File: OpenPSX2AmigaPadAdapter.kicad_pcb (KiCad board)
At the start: 2 copper layers, 58.9 x 44.2 mm, 36 parts, among them J1 TO_PSX_PAD, J2 DB9_F, J3 CONN_FTDI, J4 CONN_ICSP, J99 OSHW_LOGO, Q1 BSS138, Q2 BSS138, Q3 BSS138, Q4 BSS138, SW1 RESET, U1 ATmega328P-AU, U2 LM1117-3.3, Y1 16MHz

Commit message: Add license
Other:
- board text added: "Licensed under CERN OHL v.1.2"
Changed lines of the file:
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@@
   (general
     (thickness 1.6)
-    (drawings 26)
-    (tracks 340)
+    (drawings 27)
+    (tracks 339)
     (zones 0)
     (modules 36)
@@
   (title_block
     (title OpenPSX2AmigaPadAdapter)
-    (date 2019-09-11)
+    (date 2019-09-14)
     (rev 1git)
     (company SukkoPera)
+    (comment 1 "Licensed under CERN OHL v.1.2")
   )
   (layers
@@
     )
   )
+  (gr_text "Licensed under CERN OHL v.1.2" (at 141.986 90.424) (layer B.SilkS)
+    (effects (font (size 1 1) (thickness 0.15)) (justify mirror))
+  )
   (gr_circle (center 143.002 79.248) (end 143.129 79.248) (layer F.SilkS) (width 0.4))
   (gr_text NC (at 132.08 90.424) (layer F.SilkS)
@@
   (segment (start 143.002 65.024) (end 142.494 64.516) (width 0.25) (layer B.Cu) (net 7))
   (segment (start 125.39 64.944) (end 131.15 64.944) (width 0.25) (layer F.Cu) (net 7))
-  (via (at 125.39 61.468) (size 0.6) (drill 0.4) (layers F.Cu B.Cu) (net 7))
-  (segment (start 125.39 61.892264) (end 125.39 64.944) (width 0.25) (layer F.Cu) (net 7))
+  (via (at 125.39 61.595) (size 0.6) (drill 0.4) (layers F.Cu B.Cu) (net 7))
   (segment (start 136.652 84.582) (end 136.652 82.677) (width 0.25) (layer F.Cu) (net 7))
   (segment (start 136.652 85.09) (end 136.652 84.582) (width 0.25) (layer F.Cu) (net 7))
   (segment (start 136.271 85.471) (end 136.652 85.09) (width 0.25) (layer F.Cu) (net 7))
   (segment (start 125.222 85.471) (end 136.271 85.471) (width 0.25) (layer F.Cu) (net 7))
-  (segment (start 125.39 61.468) (end 125.39 61.892264) (width 0.25) (layer F.Cu) (net 7))
-  (segment (start 139.7 62.103) (end 139.7 63.313919) (width 0.25) (layer B.Cu) (net 7))
-  (segment (start 139.7 63.313919) (end 139.7 64.516) (width 0.25) (layer B.Cu) (net 7))
-  (segment (start 125.349 61.468) (end 139.065 61.468) (width 0.25) (layer B.Cu) (net 7))
-  (segment (start 139.065 61.468) (end 139.7 62.103) (width 0.25) (layer B.Cu) (net 7))
+  (segment (start 139.7 62.103) (end 139.7 64.516) (width 0.25) (layer B.Cu) (net 7))
+  (segment (start 125.39 61.595) (end 139.192 61.595) (width 0.25) (layer B.Cu) (net 7))
+  (segment (start 139.192 61.595) (end 139.7 62.103) (width 0.25) (layer B.Cu) (net 7))
+  (segment (start 125.39 61.595) (end 125.39 62.017) (width 0.25) (layer F.Cu) (net 7))
+  (segment (start 125.39 61.892264) (end 125.39 62.017) (width 0.25) (layer F.Cu) (net 7))
+  (segment (start 125.39 62.017) (end 125.39 64.944) (width 0.25) (layer F.Cu) (net 7))
   (segment (start 160.02 74.8157) (end 162.3187 74.8157) (width 0.5) (layer F.Cu) (net 8))
   (segment (start 162.3187 74.8157) (end 162.8775 75.3745) (width 0.5) (layer F.Cu) (net 8))
@@
   (segment (start 128.5715 64.643) (end 128.5715 62.5635) (width 0.25) (layer B.Cu) (net 23))
   (segment (start 138.43 65.786) (end 139.7 67.056) (width 0.25) (layer B.Cu) (net 23))
-  (segment (start 129.159 61.976) (end 129.413 61.976) (width 0.25) (layer B.Cu) (net 23))
-  (segment (start 129.286 61.976) (end 129.413 61.976) (width 0.25) (layer B.Cu) (net 23))
-  (segment (start 137.668 61.976) (end 138.43 62.738) (width 0.25) (layer B.Cu) (net 23))
-  (segment (start 129.413 61.976) (end 137.668 61.976) (width 0.25) (layer B.Cu) (net 23))
-  (segment (start 128.5715 62.5635) (end 129.159 61.976) (width 0.25) (layer B.Cu) (net 23))
   (segment (start 138.43 62.738) (end 138.43 65.786) (width 0.25) (layer B.Cu) (net 23))
   (segment (start 152.146 63.246) (end 152.654 63.754) (width 0.25) (layer F.Cu) (net 23))
   (segment (start 152.654 63.754) (end 152.654 70.104) (width 0.25) (layer F.Cu) (net 23))
   (segment (start 141.986 63.246) (end 152.146 63.246) (width 0.25) (layer F.Cu) (net 23))
+  (segment (start 138.049 62.357) (end 138.43 62.738) (width 0.25) (layer B.Cu) (net 23))
+  (segment (start 137.795 62.103) (end 138.049 62.357) (width 0.25) (layer B.Cu) (net 23))
+  (segment (start 129.032 62.103) (end 137.795 62.103) (width 0.25) (layer B.Cu) (net 23))
+  (segment (start 128.5715 62.5635) (end 129.032 62.103) (width 0.25) (layer B.Cu) (net 23))
   (segment (start 135.636 67.056) (end 137.16 67.056) (width 0.25) (layer F.Cu) (net 24))
   (segment (start 135.636 67.056) (end 135.636 69.85) (width 0.25) (layer F.Cu) (net 24))

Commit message: Minor refinements
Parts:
- moved C6 0.13 mm to (140.2, 90.0)
- moved C7 0.13 mm to (147.1, 90.0)
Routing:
- net +5V: track 93.8 -> 92.9 mm
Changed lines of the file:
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@@
     (thickness 1.6)
     (drawings 27)
-    (tracks 339)
+    (tracks 338)
     (zones 0)
     (modules 36)
@@
     (46 B.CrtYd user hide)
     (47 F.CrtYd user hide)
-    (49 F.Fab user)
+    (49 F.Fab user hide)
   )
   (setup
@@
     (tags "capacitor handsolder")
     (attr smd)
-    (fp_text reference C3 (at -3.02 0 90) (layer B.SilkS)
+    (fp_text reference C3 (at -2.766 0 180) (layer B.SilkS)
       (effects (font (size 1 1) (thickness 0.15)) (justify mirror))
     )
@@
     (tags "capacitor handsolder")
     (attr smd)
-    (fp_text reference C4 (at -3.02 0 90) (layer B.SilkS)
+    (fp_text reference C4 (at -2.766 0 180) (layer B.SilkS)
       (effects (font (size 1 1) (thickness 0.15)) (justify mirror))
     )
@@
   )
   (module Capacitor_SMD:C_0805_2012Metric_Pad1.15x1.40mm_HandSolder (layer F.Cu)
-    (at 140.162 89.916)
+    (at 140.162 90.043)
     (descr "Capacitor SMD 0805 (2012 Metric), square (rectangular) end terminal, IPC_7351 nominal with elongated pad for handsoldering. (Body size source: https://docs.google.com/spreadsheets/d/1BsfQQcO9C6DZCsRaXUlFlo91Tg2WpOkGARC1WS5S8t0/edit?usp=sharing), generated with kicad-footprint-generator")
     (tags "capacitor handsolder")
@@
   )
   (module Capacitor_SMD:C_0805_2012Metric_Pad1.15x1.40mm_HandSolder (layer F.Cu)
-    (at 147.092 89.916 180)
+    (at 147.092 90.043 180)
     (descr "Capacitor SMD 0805 (2012 Metric), square (rectangular) end terminal, IPC_7351 nominal with elongated pad for handsoldering. (Body size source: https://docs.google.com/spreadsheets/d/1BsfQQcO9C6DZCsRaXUlFlo91Tg2WpOkGARC1WS5S8t0/edit?usp=sharing), generated with kicad-footprint-generator")
     (tags "capacitor handsolder")
@@
     (tags "Diode SMA (DO-214AC)")
     (attr smd)
-    (fp_text reference D1 (at -4.318 0 180) (layer F.SilkS)
+    (fp_text reference D1 (at -4.445 0 180) (layer F.SilkS)
       (effects (font (size 1 1) (thickness 0.15)))
     )
@@
   (via (at 125.857 77.5675) (size 0.8) (drill 0.6) (layers F.Cu B.Cu) (net 1))
   (via (at 150.0505 80.645) (size 0.8) (drill 0.6) (layers F.Cu B.Cu) (net 1))
-  (via (at 147.32 87.5665) (size 0.8) (drill 0.6) (layers F.Cu B.Cu) (net 1))
-  (via (at 145.034 87.5665) (size 0.8) (drill 0.6) (layers F.Cu B.Cu) (net 1))
-  (via (at 139.137 87.5665) (size 0.8) (drill 0.6) (layers F.Cu B.Cu) (net 1))
+  (via (at 148.117 88.5825) (size 0.8) (drill 0.6) (layers F.Cu B.Cu) (net 1))
+  (via (at 143.637 88.5825) (size 0.8) (drill 0.6) (layers F.Cu B.Cu) (net 1))
+  (via (at 139.137 88.5825) (size 0.8) (drill 0.6) (layers F.Cu B.Cu) (net 1))
   (via (at 139.137 81.3435) (size 0.8) (drill 0.6) (layers F.Cu B.Cu) (net 1))
   (via (at 139.065 74.422) (size 0.8) (drill 0.6) (layers F.Cu B.Cu) (net 1))
@@
   (segment (start 134.611 81.162) (end 133.359 81.162) (width 0.5) (layer B.Cu) (net 2))
   (segment (start 133.359 81.162) (end 131.191 81.162) (width 0.5) (layer B.Cu) (net 2))
-  (segment (start 133.806666 68.782666) (end 136.473666 68.782666) (width 0.5) (layer B.Cu) (net 2))
-  (segment (start 134.568666 68.782666) (end 133.806666 68.782666) (width 0.5) (layer B.Cu) (net 2))
-  (segment (start 133.806666 68.782666) (end 131.191 68.782666) (width 0.5) (layer B.Cu) (net 2))
-  (segment (start 137.16 69.469) (end 137.16 69.596) (width 0.5) (layer B.Cu) (net 2))
-  (segment (start 136.473666 68.782666) (end 137.16 69.469) (width 0.5) (layer B.Cu) (net 2))
   (via (at 133.4 81.162) (size 0.8) (drill 0.6) (layers F.Cu B.Cu) (net 2))
   (segment (start 130.57 81.162) (end 133.4 81.162) (width 0.5) (layer F.Cu) (net 2))
@@
   (segment (start 150.876 87.598) (end 152.908 87.598) (width 0.5) (layer F.Cu) (net 2))
   (segment (start 150.876 84.074) (end 150.876 87.598) (width 0.5) (layer B.Cu) (net 2))
+  (segment (start 135.144585 68.782666) (end 133.806666 68.782666) (width 0.5) (layer B.Cu) (net 2))
+  (segment (start 133.806666 68.782666) (end 131.191 68.782666) (width 0.5) (layer B.Cu) (net 2))
+  (segment (start 135.957919 69.596) (end 135.144585 68.782666) (width 0.5) (layer B.Cu) (net 2))
+  (segment (start 137.16 69.596) (end 135.957919 69.596) (width 0.5) (layer B.Cu) (net 2))
   (segment (start 124.281 65.593) (end 124.206 65.668) (width 0.5) (layer B.Cu) (net 3))
   (segment (start 126.6985 65.593) (end 124.281 65.593) (width 0.25) (layer B.Cu) (net 3))
@@
   (segment (start 124.281 81.087) (end 124.206 81.162) (width 0.5) (layer B.Cu) (net 3))
   (segment (start 126.5715 81.087) (end 124.281 81.087) (width 0.25) (layer B.Cu) (net 3))
-  (via (at 120.7645 81.162) (size 0.8) (drill 0.6) (layers F.Cu B.Cu) (net 3))
+  (via (at 120.7645 81.162) (size 0.6) (drill 0.4) (layers F.Cu B.Cu) (net 3))
   (segment (start 120.7645 65.6955) (end 120.801 65.659) (width 0.5) (layer F.Cu) (net 3))
   (segment (start 120.7645 78.9035) (end 120.7645 76.0365) (width 0.25) (layer F.Cu) (net 3))
-  (via (at 120.7645 75.997332) (size 0.8) (drill 0.6) (layers F.Cu B.Cu) (net 3))
+  (via (at 120.7645 75.997332) (size 0.6) (drill 0.4) (layers F.Cu B.Cu) (net 3))
   (segment (start 120.7645 76.0365) (end 120.7645 70.8295) (width 0.25) (layer F.Cu) (net 3))
-  (via (at 120.7645 70.832666) (size 0.8) (drill 0.6) (layers F.Cu B.Cu) (net 3))
+  (via (at 120.7645 70.832666) (size 0.6) (drill 0.4) (layers F.Cu B.Cu) (net 3))
   (segment (start 120.7645 70.8295) (end 120.7645 65.6955) (width 0.25) (layer F.Cu) (net 3))
-  (via (at 120.7645 65.668) (size 0.8) (drill 0.6) (layers F.Cu B.Cu) (net 3))
+  (via (at 120.7645 65.668) (size 0.6) (drill 0.4) (layers F.Cu B.Cu) (net 3))
   (segment (start 120.7645 78.9035) (end 120.7645 81.1165) (width 0.25) (layer F.Cu) (net 3))
   (segment (start 122.2645 81.162) (end 124.206 81.162) (width 0.25) (layer B.Cu) (net 3))

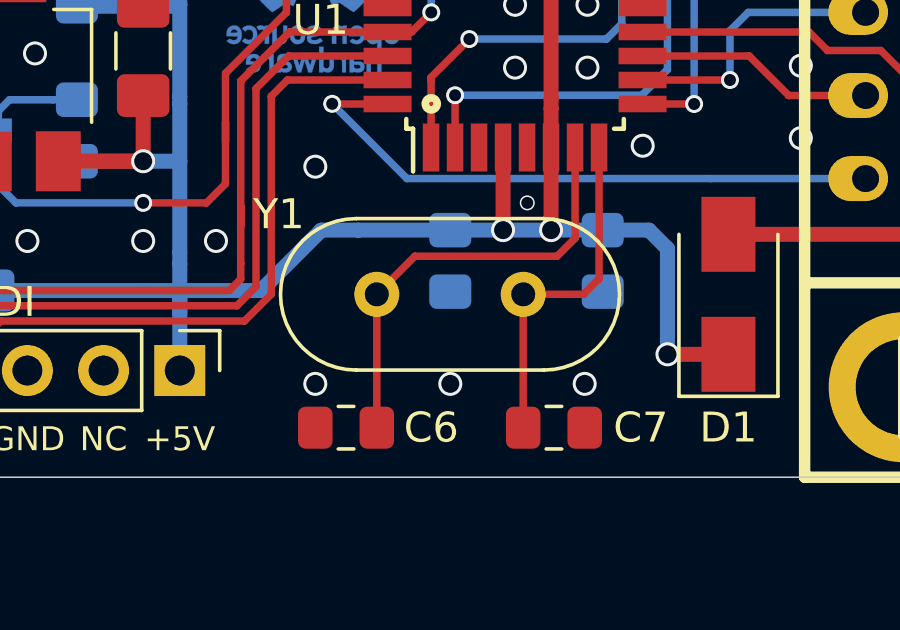
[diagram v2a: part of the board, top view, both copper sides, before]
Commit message: Add footprint for SMD resonator
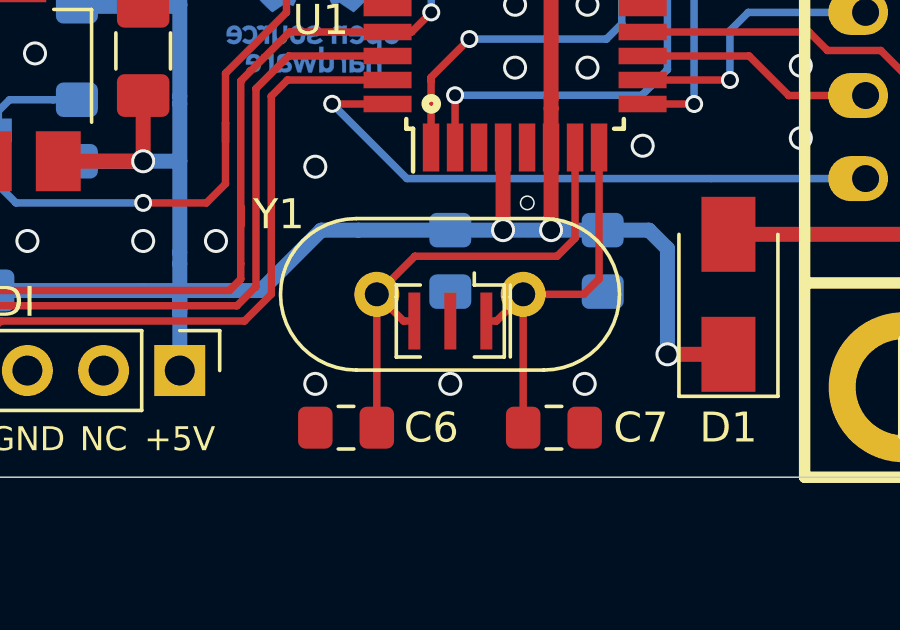
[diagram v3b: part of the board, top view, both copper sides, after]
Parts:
- added Y2: 16M, Crystal:Resonator_SMD_muRata_CSTxExxV-3Pin_3.0x1.1mm, F.Cu at (143.6, 86.5)
- Y1: value 16MHz -> 16M
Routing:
- net Net-(C6-Pad2): track 14.7 -> 16.3 mm
- net Net-(C7-Pad2): track 11.4 -> 13.0 mm
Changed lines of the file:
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@@
     (thickness 1.6)
     (drawings 27)
-    (tracks 338)
+    (tracks 342)
     (zones 0)
-    (modules 36)
+    (modules 37)
     (nets 31)
   )
@@
       (effects (font (size 1 1) (thickness 0.15)))
     )
-    (fp_text value 16MHz (at 2.44 3.525) (layer F.Fab)
+    (fp_text value 16M (at 2.44 3.525) (layer F.Fab)
       (effects (font (size 1 1) (thickness 0.15)))
     )
@@
     )
   )
+  (module Crystal:Resonator_SMD_muRata_CSTxExxV-3Pin_3.0x1.1mm (layer F.Cu)
+    (at 143.637 86.487 180)
+    (descr "SMD Resomator/Filter Murata CSTCE, https://www.murata.com/en-eu/products/productdata/8801162264606/SPEC-CSTNE16M0VH3C000R0.pdf")
+    (tags "SMD SMT ceramic resonator filter")
+    (attr smd)
+    (fp_text reference Y2 (at 0 -2) (layer F.SilkS) hide
+      (effects (font (size 1 1) (thickness 0.15)))
+    )
+    (fp_text value 16M (at 0 1.8) (layer F.Fab)
+      (effects (font (size 0.2 0.2) (thickness 0.03)))
+    )
+    (fp_text user %R (at 0.1 -0.05) (layer F.Fab)
+      (effects (font (size 0.6 0.6) (thickness 0.08)))
+    )
+    (fp_line (start 1.8 1.2) (end 1 1.2) (layer F.SilkS) (width 0.12))
+    (fp_line (start 1.8 -1.2) (end 1.8 0.8) (layer F.SilkS) (width 0.12))
+    (fp_line (start 1 -1.2) (end 1.8 -1.2) (layer F.SilkS) (width 0.12))
+    (fp_line (start -1.8 -1.2) (end -0.8 -1.2) (layer F.SilkS) (width 0.12))
+    (fp_line (start -1.8 0.8) (end -1.8 -1.2) (layer F.SilkS) (width 0.12))
+    (fp_line (start -0.8 1.2) (end -1.8 1.2) (layer F.SilkS) (width 0.12))
+    (fp_line (start -0.8 1.2) (end -0.8 1.6) (layer F.SilkS) (width 0.12))
+    (fp_line (start -2 -1.2) (end -2 0.8) (layer F.SilkS) (width 0.12))
+    (fp_line (start 1.8 0.8) (end 1.8 1.2) (layer F.SilkS) (width 0.12))
+    (fp_line (start -1.8 0.8) (end -1.8 1.2) (layer F.SilkS) (width 0.12))
+    (fp_line (start -2 0.8) (end -2 1.2) (layer F.SilkS) (width 0.12))
+    (fp_line (start 1.5 0.8) (end 1.5 -0.8) (layer F.Fab) (width 0.1))
+    (fp_line (start 1.5 -0.8) (end -1.5 -0.8) (layer F.Fab) (width 0.1))
+    (fp_line (start -1 0.8) (end -1.5 0.3) (layer F.Fab) (width 0.1))
+    (fp_line (start -1 0.8) (end 1.5 0.8) (layer F.Fab) (width 0.1))
+    (fp_line (start -1.5 0.3) (end -1.5 -0.8) (layer F.Fab) (width 0.1))
+    (fp_line (start 1.75 1.2) (end -1.75 1.2) (layer F.CrtYd) (width 0.05))
+    (fp_line (start -1.75 -1.2) (end 1.75 -1.2) (layer F.CrtYd) (width 0.05))
+    (fp_line (start 1.75 -1.2) (end 1.75 1.2) (layer F.CrtYd) (width 0.05))
+    (fp_line (start -1.75 1.2) (end -1.75 -1.2) (layer F.CrtYd) (width 0.05))
+    (pad 1 smd rect (at -1.2 0 180) (size 0.4 1.9) (layers F.Cu F.Paste F.Mask)
+      (net 5 "Net-(C7-Pad2)"))
+    (pad 2 smd rect (at 0 0 180) (size 0.4 1.9) (layers F.Cu F.Paste F.Mask)
+      (net 1 GND))
+    (pad 3 smd rect (at 1.2 0 180) (size 0.4 1.9) (layers F.Cu F.Paste F.Mask)
+      (net 4 "Net-(C6-Pad2)"))
+    (model ${KISYS3DMOD}/Crystal.3dshapes/Resonator_SMD_muRata_CSTxExxV-3Pin_3.0x1.1mm.wrl
+      (at (xyz 0 0 0))
+      (scale (xyz 1 1 1))
+      (rotate (xyz 0 0 0))
+    )
+  )
   (gr_text "Licensed under CERN OHL v.1.2" (at 141.986 90.424) (layer B.SilkS)
     (effects (font (size 1 1) (thickness 0.15)) (justify mirror))
@@
   (segment (start 147.796 83.731002) (end 147.199002 84.328) (width 0.25) (layer F.Cu) (net 4))
   (segment (start 147.796 80.704) (end 147.796 83.731002) (width 0.25) (layer F.Cu) (net 4))
+  (segment (start 142.076 86.487) (end 141.187 85.598) (width 0.25) (layer F.Cu) (net 4))
+  (segment (start 142.437 86.487) (end 142.076 86.487) (width 0.25) (layer F.Cu) (net 4))
   (segment (start 146.067 85.598) (end 146.067 89.916) (width 0.25) (layer F.Cu) (net 5))
   (segment (start 148.596 85.084) (end 148.082 85.598) (width 0.25) (layer F.Cu) (net 5))
   (segment (start 148.082 85.598) (end 146.067 85.598) (width 0.25) (layer F.Cu) (net 5))
   (segment (start 148.596 80.704) (end 148.596 85.084) (width 0.25) (layer F.Cu) (net 5))
+  (segment (start 145.178 86.487) (end 146.067 85.598) (width 0.25) (layer F.Cu) (net 5))
+  (segment (start 144.837 86.487) (end 145.178 86.487) (width 0.25) (layer F.Cu) (net 5))
   (segment (start 121.92 85.471) (end 121.92 88.138) (width 0.25) (layer B.Cu) (net 6))
   (via (at 143.002 76.2) (size 0.6) (drill 0.4) (layers F.Cu B.Cu) (net 7))

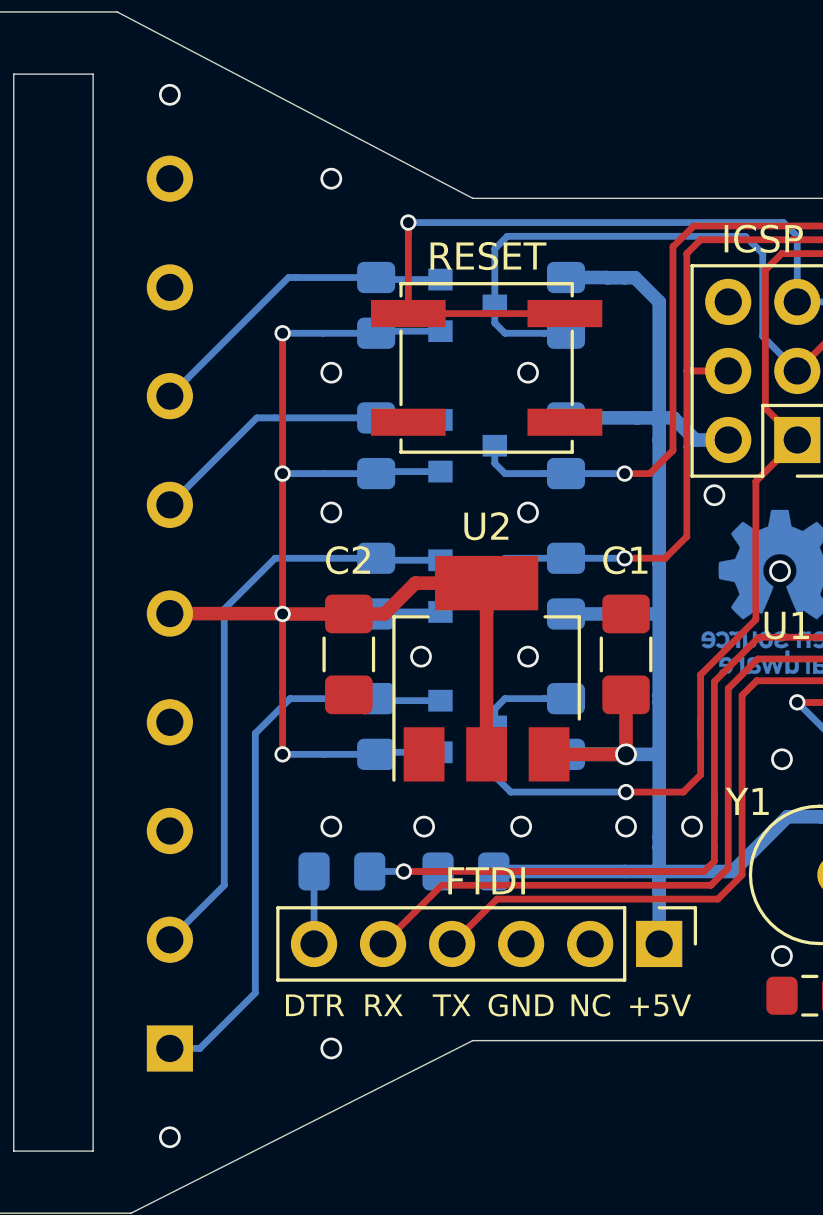
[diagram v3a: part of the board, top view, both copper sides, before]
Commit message: Add pull-up resistors on DATA and ACK
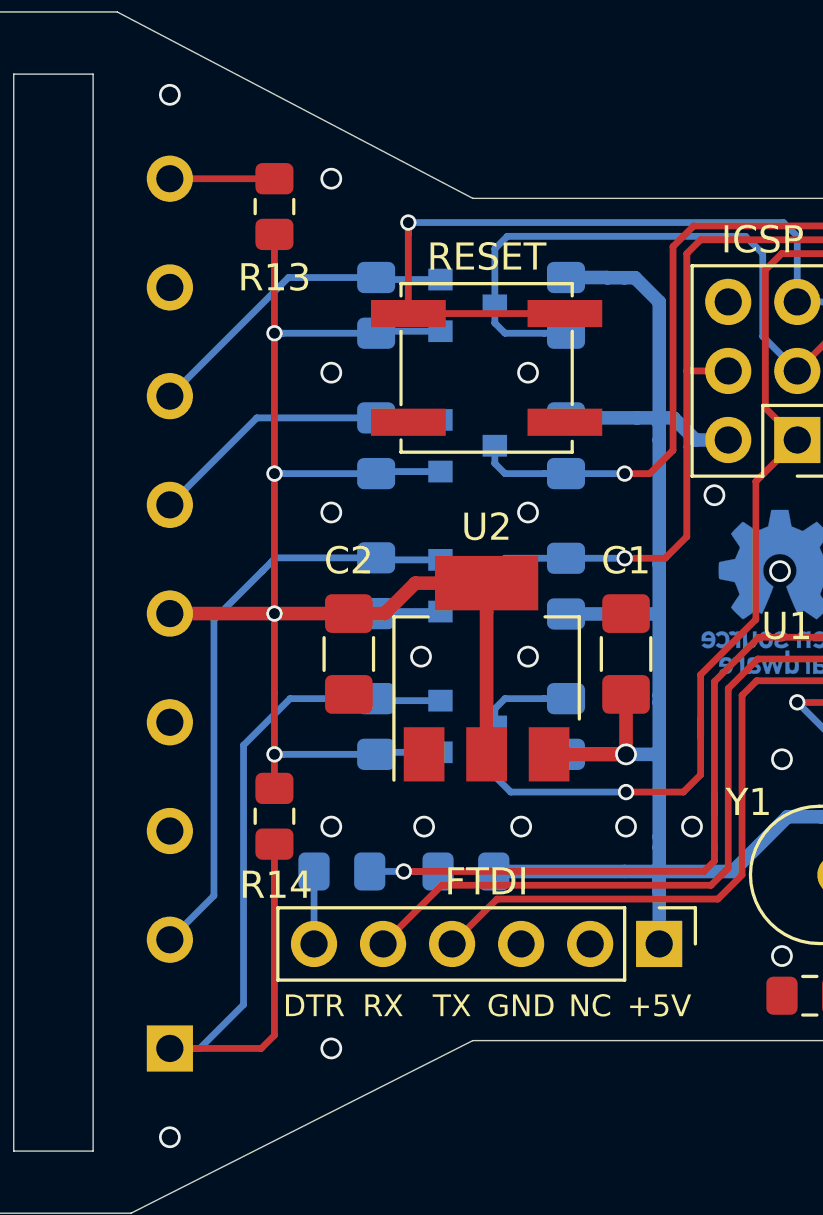
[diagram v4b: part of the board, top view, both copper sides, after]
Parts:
- added R13: 10k, Resistor_SMD:R_0805_2012Metric_Pad1.15x1.40mm_HandSolder, F.Cu at (120.5, 61.0)
- added R14: 10k, Resistor_SMD:R_0805_2012Metric_Pad1.15x1.40mm_HandSolder, F.Cu at (120.5, 83.4)
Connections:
- J1 pad 9: (no net) -> /ps_ack_3v3
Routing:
- net /ps_data_3v3: track 20.9 -> 32.0 mm
- net +3V3: track 57.4 -> 63.5 mm
- net /ps_ack_3v3: track 0.00 -> 3.85 mm
